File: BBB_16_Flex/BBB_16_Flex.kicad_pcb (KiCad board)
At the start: 2 copper layers, 162.6 x 59.2 mm, 36 parts, among them J1 Output 1, J2 Output 2, J3 Output 3, J4 RTC Conn, J5 OLED Conn, J7 DMX1, J8 DMX2, J9 Power Select, SW1 PWR_BUTTON, SW2 Up BTN, SW3 Down/Test BTN, SW4 Back BTN, SW5 Enter BTN, U1 BEAGLEBONEBLACK, U2 UA9638CP, U3 24LC256

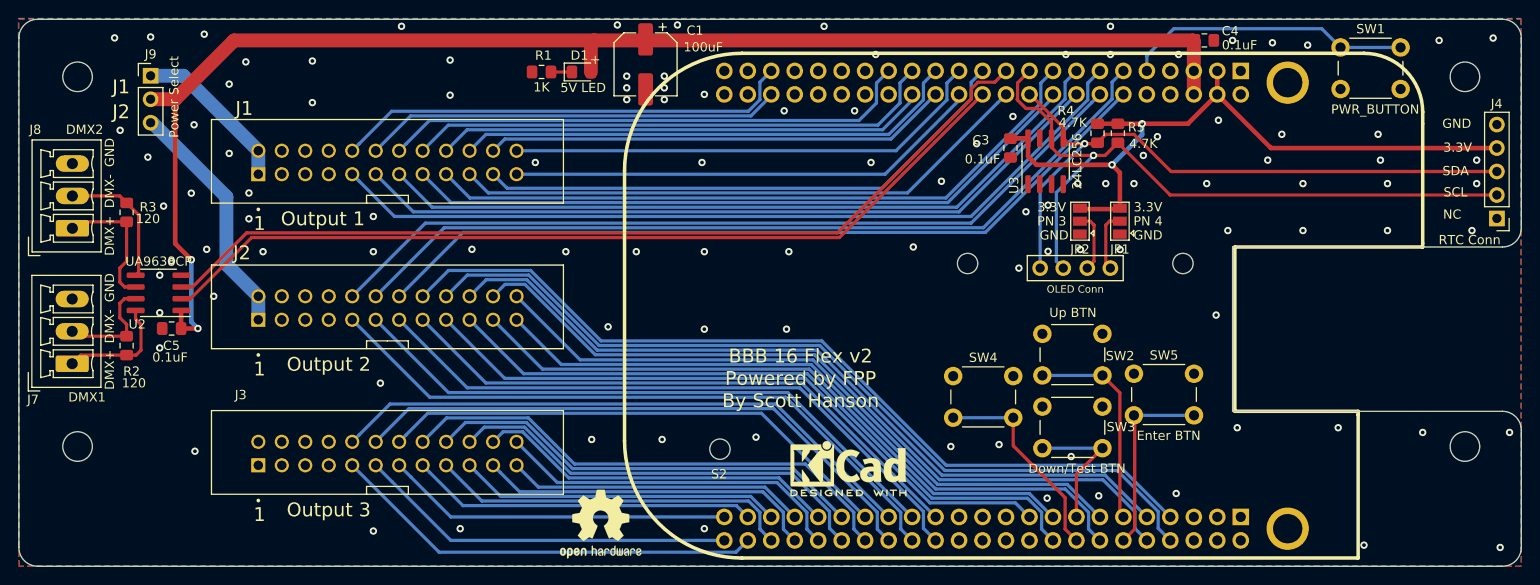
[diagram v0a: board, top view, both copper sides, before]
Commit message: upgrade PCB to v6
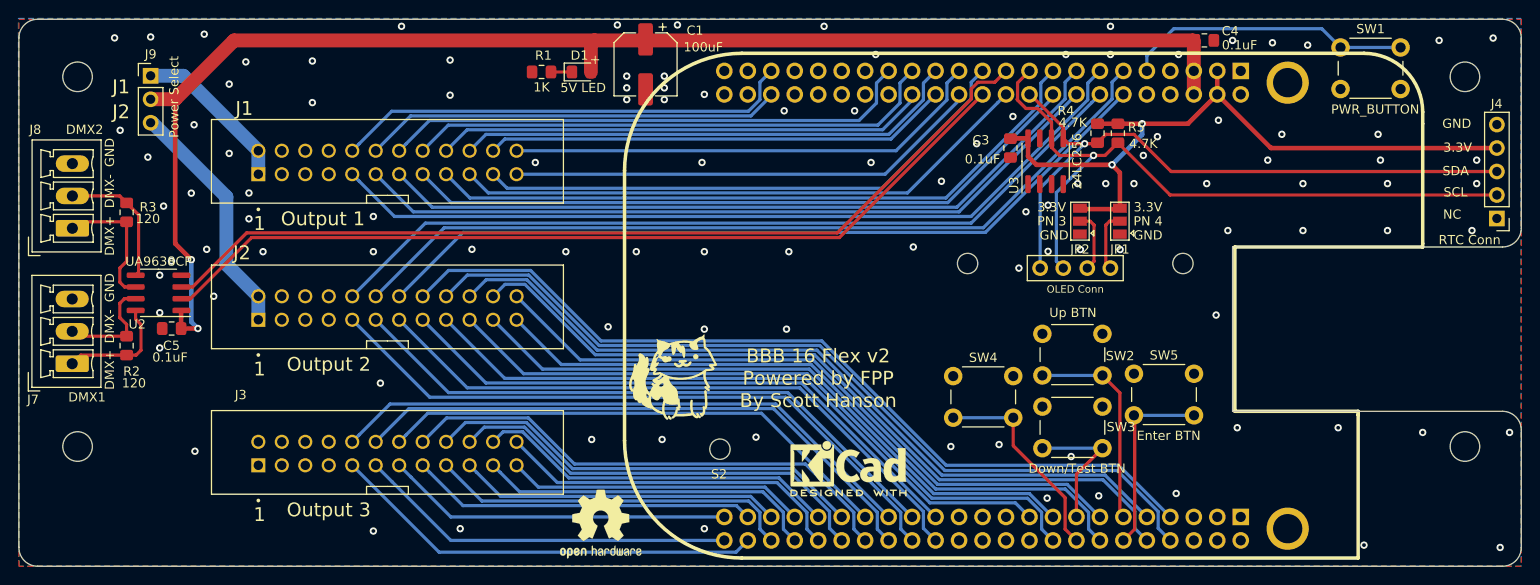
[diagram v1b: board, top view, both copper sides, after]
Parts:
- added G***: LOGO, Scotts:chewi_15, F.Cu at (156.9, 108.7)
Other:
- net class 3.3v removed
- net class 5v removed
- net class Default removed
- net class Gnd removed
- net class Power removed
- net class Vin removed
- net class power2 removed
- net class usb removed

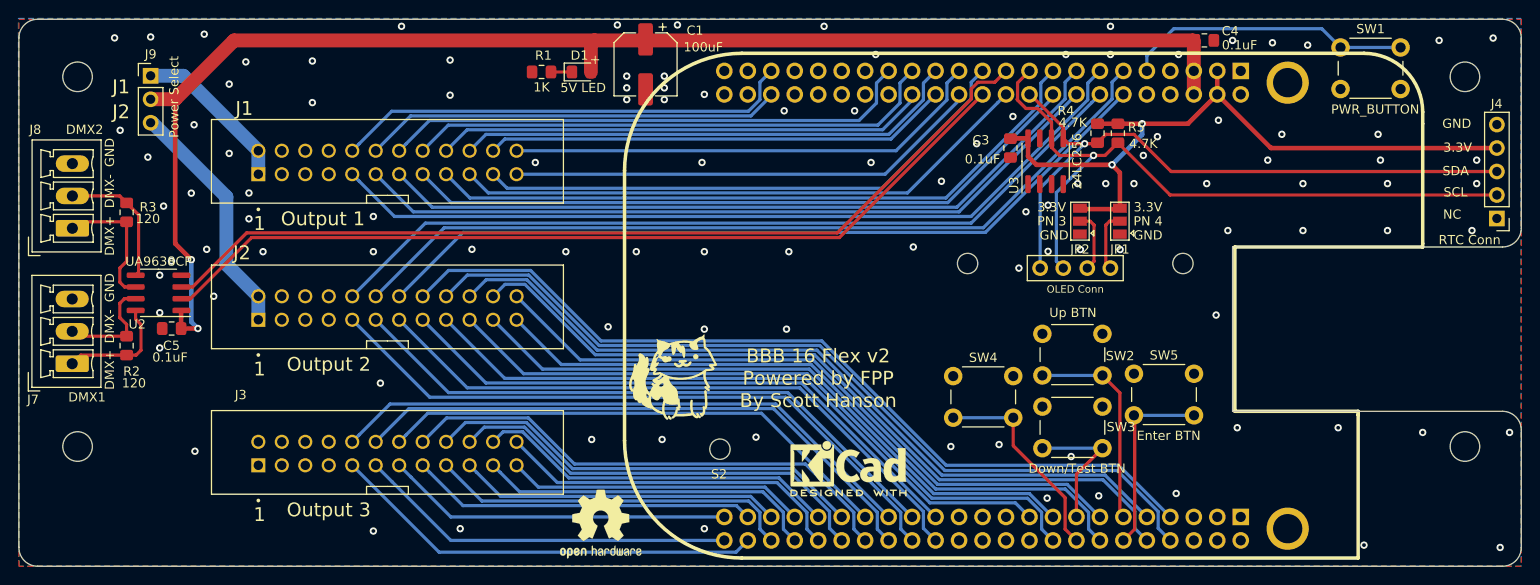
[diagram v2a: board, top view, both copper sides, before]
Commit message: added BBB_16_Flex
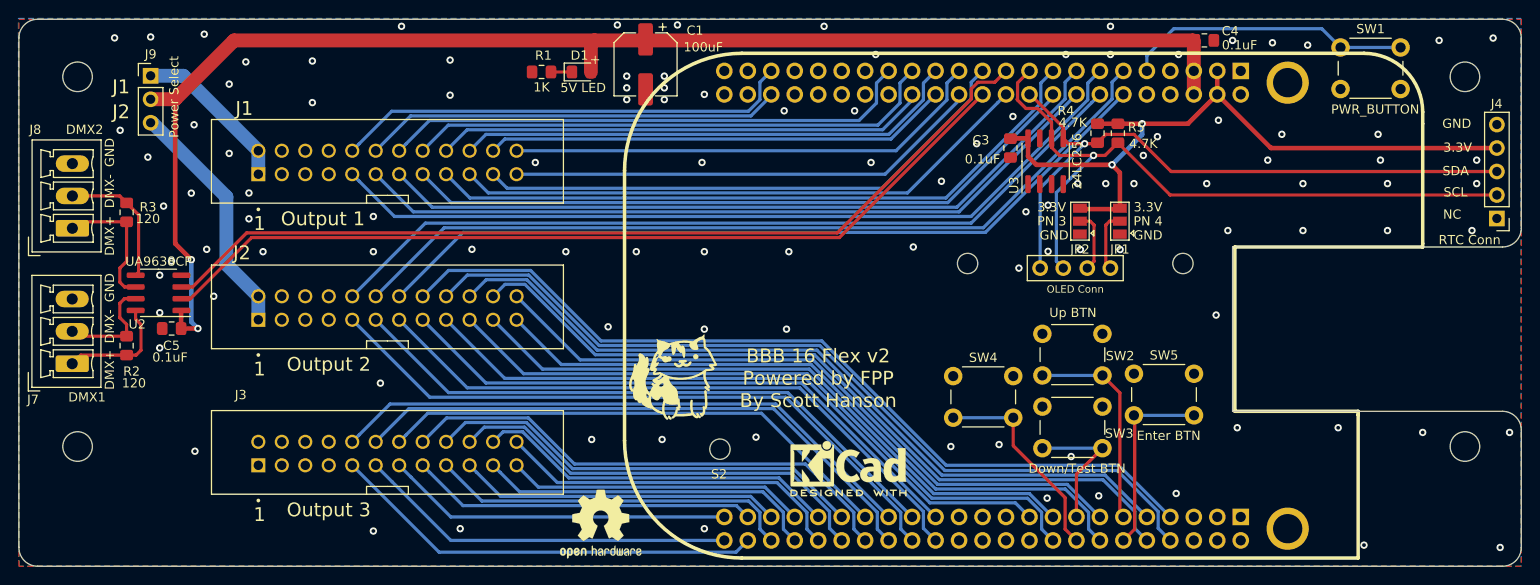
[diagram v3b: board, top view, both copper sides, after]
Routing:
- net /Serial/DMX2-: track 15.8 -> 14.7 mm
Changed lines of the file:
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@@
     (tags "tact sw push 6mm")
     (attr through_hole)
-    (fp_text reference "SW3" (at 8.5 2.2) (layer "F.SilkS")
+    (fp_text reference "SW3" (at 8.312 2.904) (layer "F.SilkS")
       (effects (font (size 1 1) (thickness 0.15)))
     )
@@
   (segment (start 98.015 93.0332) (end 92.8498 93.0332) (width 0.35) (layer "F.Cu") (net 27))
   (segment (start 92.8498 93.0332) (end 92.1476 93.7354) (width 0.35) (layer "F.Cu") (net 27))
-  (segment (start 92.15268 93.73032) (end 92.173 93.71) (width 0.35) (layer "F.Cu") (net 27))
   (segment (start 97.282 98.044) (end 98.015 97.311) (width 0.35) (layer "F.Cu") (net 27))
-  (segment (start 92.5921 93.7227) (end 92.58448 93.73032) (width 0.35) (layer "F.Cu") (net 27))
   (segment (start 98.015 97.311) (end 98.015 93.0332) (width 0.35) (layer "F.Cu") (net 27))
   (segment (start 97.282 99.568) (end 97.282 98.044) (width 0.35) (layer "F.Cu") (net 27))
   (segment (start 98.9944 100.0854) (end 97.7994 100.0854) (width 0.35) (layer "F.Cu") (net 27))
-  (segment (start 92.58448 93.73032) (end 92.15268 93.73032) (width 0.35) (layer "F.Cu") (net 27))
   (segment (start 99.314 98.4958) (end 99.314 92.2822) (width 0.35) (layer "F.Cu") (net 28))
-  (segment (start 92.33048 90.23032) (end 93.48448 90.23032) (width 0.35) (layer "F.Cu") (net 28))
   (segment (start 98.9944 98.8154) (end 99.314 98.4958) (width 0.35) (layer "F.Cu") (net 28))
   (segment (start 97.2672 90.2354) (end 98.015 90.9832) (width 0.35) (layer "F.Cu") (net 28))

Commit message: update to kicad v9
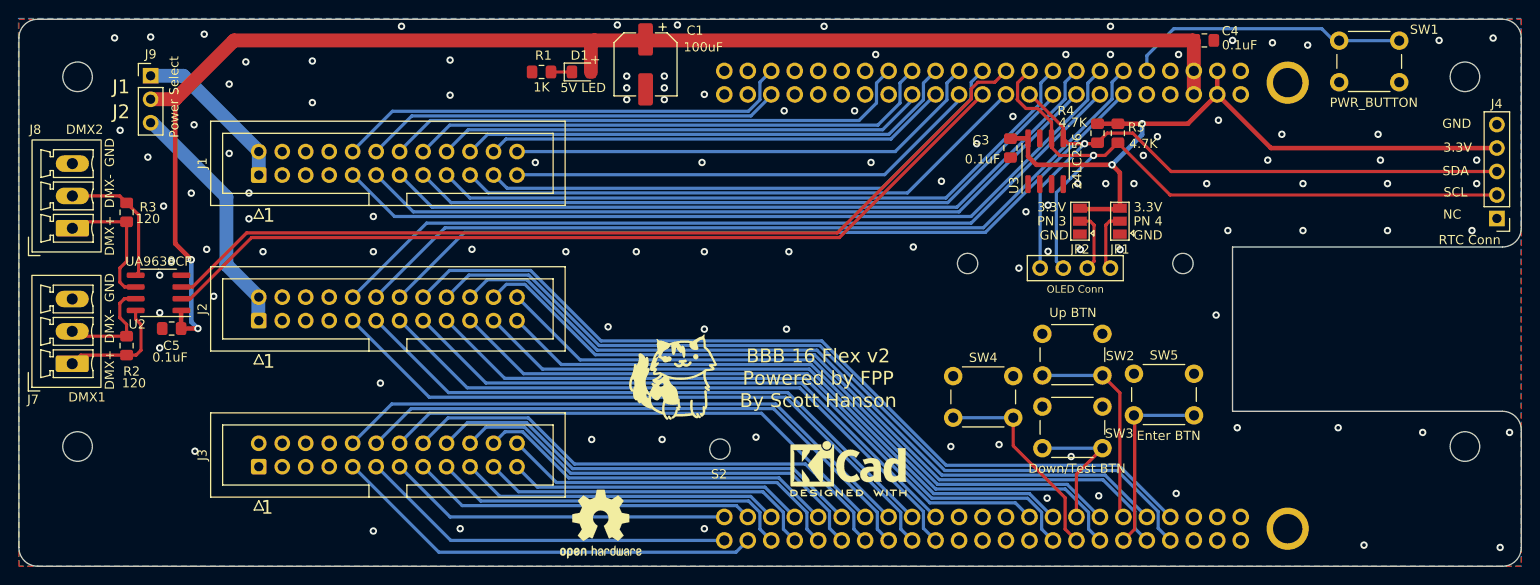
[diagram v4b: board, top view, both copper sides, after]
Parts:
- J1, J2, J3: footprint 302-S241:OST_302-S241 -> Connector_IDC:IDC-Header_2x12_P2.54mm_Vertical
- U1: footprint beagleboneblack:BEAGLEBONEBLACK -> Scotts:BEAGLEBONEBLACK
- moved J3 14.0 mm to (112.3, 119.5), turned to 90 degrees
- moved J1 14.0 mm to (112.3, 88.0), turned to 90 degrees
- moved J2 14.0 mm to (112.3, 103.7), turned to 90 degrees
- moved SW1 0.75 mm to (229.2, 73.4)

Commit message: fix
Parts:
- C3, C4, C5: footprint Capacitor_SMD:C_0805_2012Metric_Pad1.15x1.40mm_HandSolder -> Capacitor_SMD:C_0805_2012Metric
- D1: footprint LED_SMD:LED_0805_2012Metric_Pad1.15x1.40mm_HandSolder -> LED_SMD:LED_0805_2012Metric
- R1, R2, R3, R4, R5: footprint Resistor_SMD:R_0805_2012Metric_Pad1.15x1.40mm_HandSolder -> Resistor_SMD:R_0805_2012Metric
